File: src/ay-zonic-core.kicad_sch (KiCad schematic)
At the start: 31 parts, among them J1 01x10, SW1 SW_DIP_x01, U1 AY-3-8912, U2 74HCT74, U3 74HCT08, U4 74HCT11, U5 74HCT02

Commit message: added 3d model for edge connector and footprints plus added schematic to pcb.
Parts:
- CO1: footprint ZX81_FOOTPRINT:EDGE ZX81 TOP -> ZX81_Expansion_Connector:ZX81_EdgeConnector; symbol connector zx81:Connector ZX81 -> ZX81_Expansion_Connector:Connector ZX81
- CO2: footprint AudioJack:CONN5_SPC21348_MTC -> audio_jack:CONN5_SPC21348_MTC; symbol AudioJack:SPC21348 -> Stereo_Jack_Connector:SPC21348
- J1: footprint (none) -> Connector_PinHeader_2.54mm:PinHeader_1x10_P2.54mm_Vertical
- SW1: footprint Button_Switch_SMD:SW_DIP_SPSTx01_Slide_9.78x4.72mm_W8.61mm_P2.54mm -> Button_Switch_THT:SW_DIP_SPSTx01_Slide_9.78x4.72mm_W7.62mm_P2.54mm
- U1: symbol AY-3-8912:AY-3-8912 -> AY-38912:AY-3-8912
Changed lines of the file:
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@@
 	)
 	(symbol
-		(lib_id "AY-3-8912:AY-3-8912")
+		(lib_id "AY-38912:AY-3-8912")
 		(at 130.81 168.91 0)
 		(unit 1)
@@
 			)
 		)
-		(property "Footprint" ""
+		(property "Footprint" "Connector_PinHeader_2.54mm:PinHeader_1x10_P2.54mm_Vertical"
 			(at 40.64 257.81 0)
 			(effects
@@
 	)
 	(symbol
-		(lib_id "AudioJack:SPC21348")
+		(lib_id "Stereo_Jack_Connector:SPC21348")
 		(at 307.34 180.34 0)
 		(unit 1)
@@
 			)
 		)
-		(property "Footprint" "AudioJack:CONN5_SPC21348_MTC"
+		(property "Footprint" "audio_jack:CONN5_SPC21348_MTC"
 			(at 307.34 180.34 0)
 			(effects
@@
 			)
 		)
-		(property "Footprint" "Button_Switch_SMD:SW_DIP_SPSTx01_Slide_9.78x4.72mm_W8.61mm_P2.54mm"
+		(property "Footprint" "Button_Switch_THT:SW_DIP_SPSTx01_Slide_9.78x4.72mm_W7.62mm_P2.54mm"
 			(at 243.84 68.58 0)
 			(effects
@@
 	)
 	(symbol
-		(lib_id "connector zx81:Connector ZX81")
+		(lib_id "ZX81_Expansion_Connector:Connector ZX81")
 		(at 48.26 63.5 0)
 		(unit 1)
@@
 			)
 		)
-		(property "Footprint" "ZX81_FOOTPRINT:EDGE ZX81 TOP"
+		(property "Footprint" "ZX81_Expansion_Connector:ZX81_EdgeConnector"
 			(at 48.26 59.69 0)
 			(effects

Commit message: Signed-off-by: jgratton72 <jon@grattons.co.uk>
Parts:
- U2, U3, U4, U5: footprint Package_DIP:DIP-14_W7.62mm_Socket_LongPads -> Package_DIP:DIP-14_W7.62mm_LongPads
- renumbered R11 to R8, R10 to R9
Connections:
- net IOA0: now also J1.2 (Pin_2); no longer J1.1 (Pin_1)
- net IOA1: now also J1.3 (Pin_3); no longer J1.2 (Pin_2)
- net IOA2: now also J1.4 (Pin_4); no longer J1.3 (Pin_3)
- net IOA3: now also J1.5 (Pin_5); no longer J1.4 (Pin_4)
- net IOA4: now also J1.6 (Pin_6); no longer J1.5 (Pin_5)
- net IOA5: now also J1.7 (Pin_7); no longer J1.6 (Pin_6)
- net IOA6: now also J1.8 (Pin_8); no longer J1.7 (Pin_7)
- net IOA7: now also J1.9 (Pin_9); no longer J1.8 (Pin_8)
- net VCC: now also J1.1 (Pin_1); no longer J1.9 (Pin_9)

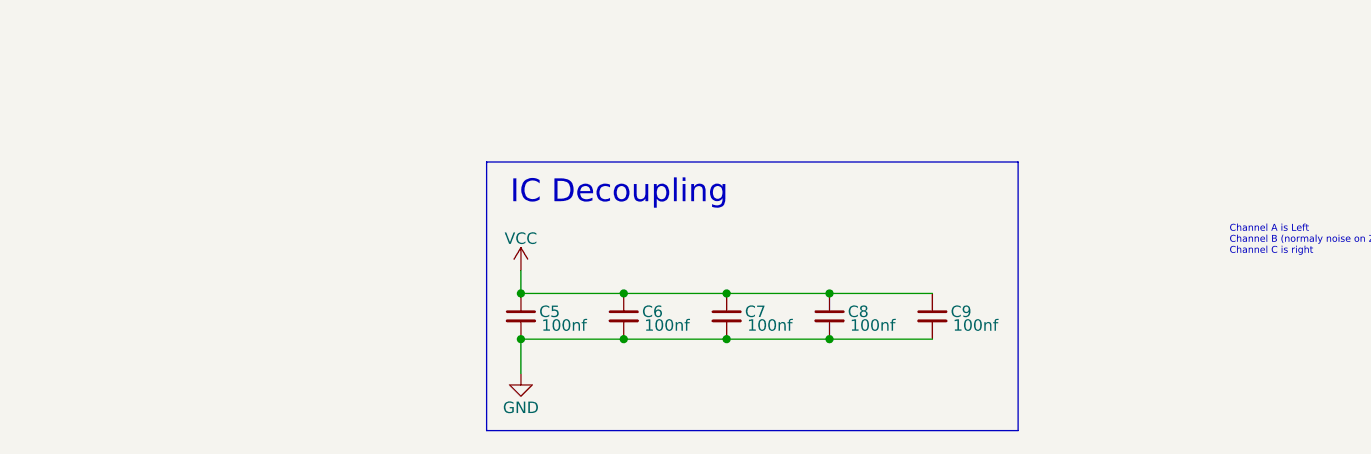
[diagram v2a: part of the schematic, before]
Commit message: added mounting holes and started routing.
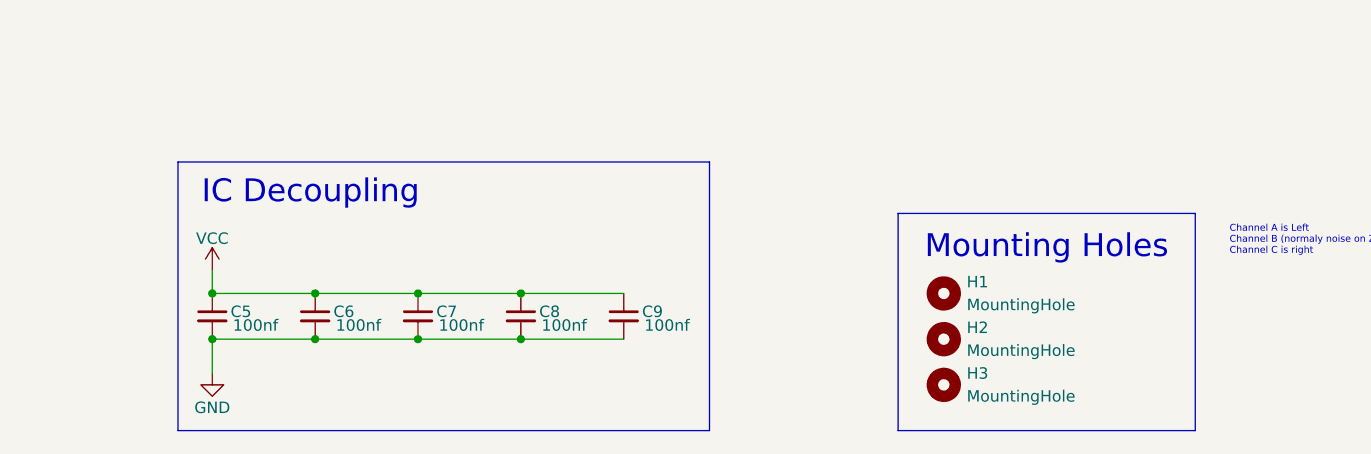
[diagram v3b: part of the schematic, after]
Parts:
- added H1, H2, H3: MountingHole, MountingHole:MountingHole_3.2mm_M3_DIN965_Pad, symbol Mechanical:MountingHole
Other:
- note added: "Mounting Holes"
- moved on the sheet: C5, C6, C7, C8, C9

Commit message: final route rev 2.0
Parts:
- added H4: MountingHole, MountingHole:MountingHole_3.2mm_M3_DIN965_Pad, symbol Mechanical:MountingHole
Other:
- moved on the sheet: H1, H2, H3
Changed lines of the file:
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@@
 	)
 	(rectangle
-		(start 264.16 254)
+		(start 264.16 250.19)
 		(end 297.18 278.13)
 		(stroke
@@
 	(text "Mounting Holes"
 		(exclude_from_sim no)
-		(at 280.67 257.81 0)
+		(at 280.67 254 0)
 		(effects
 			(font
@@
 	(symbol
 		(lib_id "Mechanical:MountingHole")
-		(at 269.24 273.05 0)
+		(at 269.24 269.24 0)
 		(unit 1)
 		(exclude_from_sim no)
@@
 		(fields_autoplaced yes)
 		(property "Reference" "H3"
-			(at 271.78 271.7799 0)
+			(at 271.78 267.9699 0)
 			(effects
 				(font
@@
 		)
 		(property "Value" "MountingHole"
-			(at 271.78 274.3199 0)
+			(at 271.78 270.5099 0)
 			(effects
 				(font
@@
 		)
 		(property "Footprint" "MountingHole:MountingHole_3.2mm_M3_DIN965_Pad"
-			(at 269.24 273.05 0)
+			(at 269.24 269.24 0)
 			(effects
 				(font
@@
 		)
 		(property "Datasheet" "~"
-			(at 269.24 273.05 0)
+			(at 269.24 269.24 0)
 			(effects
 				(font
@@
 		)
 		(property "Description" "Mounting Hole without connection"
-			(at 269.24 273.05 0)
+			(at 269.24 269.24 0)
 			(effects
 				(font
@@
 	(symbol
 		(lib_id "Mechanical:MountingHole")
-		(at 269.24 267.97 0)
+		(at 269.24 264.16 0)
 		(unit 1)
 		(exclude_from_sim no)
@@
 		(fields_autoplaced yes)
 		(property "Reference" "H2"
-			(at 271.78 266.6999 0)
+			(at 271.78 262.8899 0)
 			(effects
 				(font
@@
 		)
 		(property "Value" "MountingHole"
-			(at 271.78 269.2399 0)
+			(at 271.78 265.4299 0)
 			(effects
 				(font
@@
 		)
 		(property "Footprint" "MountingHole:MountingHole_3.2mm_M3_DIN965_Pad"
-			(at 269.24 267.97 0)
+			(at 269.24 264.16 0)
 			(effects
 				(font
@@
 		)
 		(property "Datasheet" "~"
-			(at 269.24 267.97 0)
+			(at 269.24 264.16 0)
 			(effects
 				(font
@@
 		)
 		(property "Description" "Mounting Hole without connection"
-			(at 269.24 267.97 0)
+			(at 269.24 264.16 0)
 			(effects
 				(font
@@
 	)
 	(symbol
+		(lib_id "Mechanical:MountingHole")
+		(at 269.24 274.32 0)
+		(unit 1)
+		(exclude_from_sim no)
+		(in_bom no)
+		(on_board yes)
+		(dnp no)
+		(fields_autoplaced yes)
+		(property "Reference" "H4"
+			(at 271.78 273.0499 0)
+			(effects
+				(font
+					(size 1.27 1.27)
+				)
+				(justify left)
+			)
+		)
+		(property "Value" "MountingHole"
+			(at 271.78 275.5899 0)
+			(effects
+				(font
+					(size 1.27 1.27)
+				)
+				(justify left)
+			)
+		)
+		(property "Footprint" "MountingHole:MountingHole_3.2mm_M3_DIN965_Pad"
+			(at 269.24 274.32 0)
+			(effects
+				(font
+					(size 1.27 1.27)
+				)
+				(hide yes)
+			)
+		)
+		(property "Datasheet" "~"
+			(at 269.24 274.32 0)
+			(effects
+				(font
+					(size 1.27 1.27)
+				)
+				(hide yes)
+			)
+		)
+		(property "Description" "Mounting Hole without connection"
+			(at 269.24 274.32 0)
+			(effects
+				(font
+					(size 1.27 1.27)
+				)
+				(hide yes)
+			)
+		)
+		(instances
+			(project "ay-zonic-core"
+				(path "/315d6d04-4d18-4e55-a11c-aa8b11bc2d55"
+					(reference "H4")
+					(unit 1)
+				)
+			)
+		)
+	)
+	(symbol
 		(lib_id "power:VCC")
 		(at 187.96 260.35 0)
@@
 	(symbol
 		(lib_id "Mechanical:MountingHole")
-		(at 269.24 262.89 0)
+		(at 269.24 259.08 0)
 		(unit 1)
 		(exclude_from_sim no)
@@
 		(fields_autoplaced yes)
 		(property "Reference" "H1"
-			(at 271.78 261.6199 0)
+			(at 271.78 257.8099 0)
 			(effects
 				(font
@@
 		)
 		(property "Value" "MountingHole"
-			(at 271.78 264.1599 0)
+			(at 271.78 260.3499 0)
 			(effects
 				(font
@@
 		)
 		(property "Footprint" "MountingHole:MountingHole_3.2mm_M3_DIN965_Pad"
-			(at 269.24 262.89 0)
+			(at 269.24 259.08 0)
 			(effects
 				(font
@@
 		)
 		(property "Datasheet" "~"
-			(at 269.24 262.89 0)
+			(at 269.24 259.08 0)
 			(effects
 				(font
@@
 		)
 		(property "Description" "Mounting Hole without connection"
-			(at 269.24 262.89 0)
+			(at 269.24 259.08 0)
 			(effects
 				(font
